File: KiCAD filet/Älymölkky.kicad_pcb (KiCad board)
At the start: 2 copper layers, 44 parts, among them P0.18_TP1 Conn_01x01_Male, U1 nRF52810-QCxx, X1 32MHz Crystal, X1_C1 12pF, X1_C2 12pF, X2 32.768 kHz Crystal, X2_C11 12pF, X2_C12 12pF

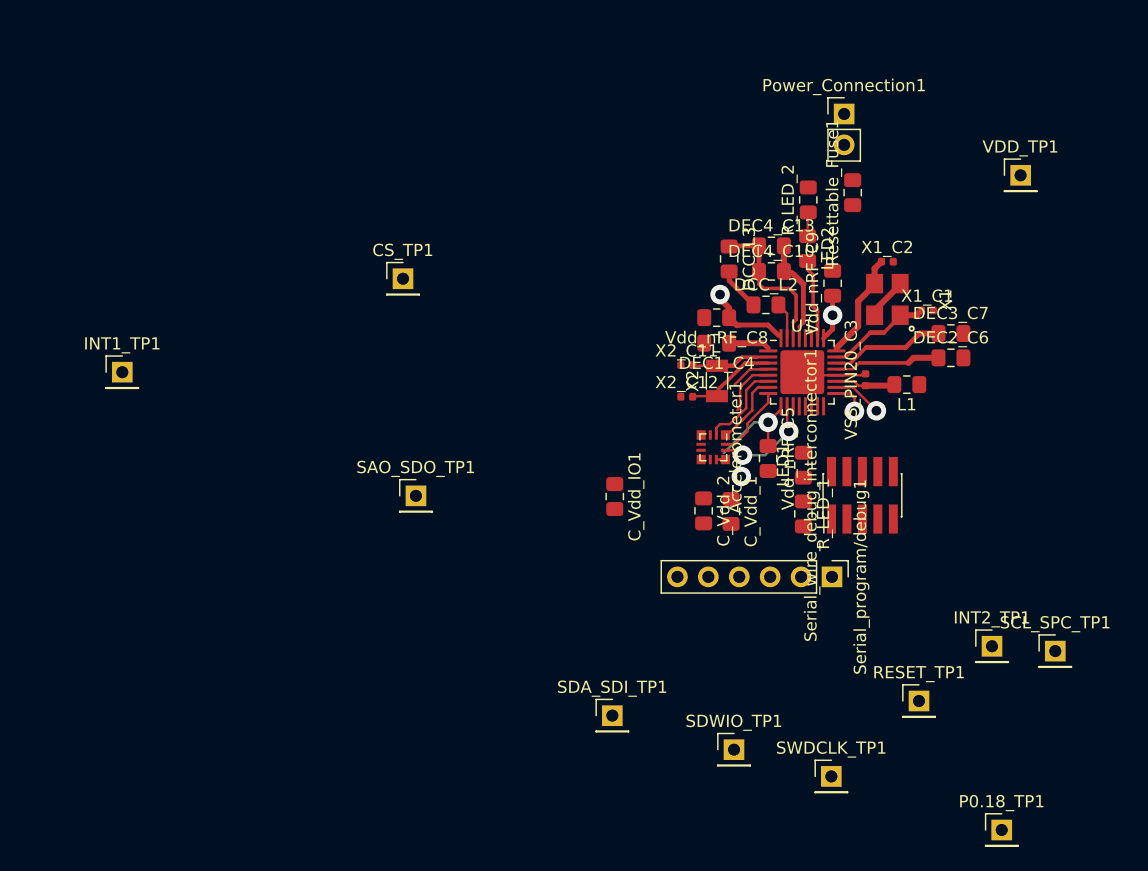
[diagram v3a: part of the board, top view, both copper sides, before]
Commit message: Drew most of remaining traces, missing antenna and switch
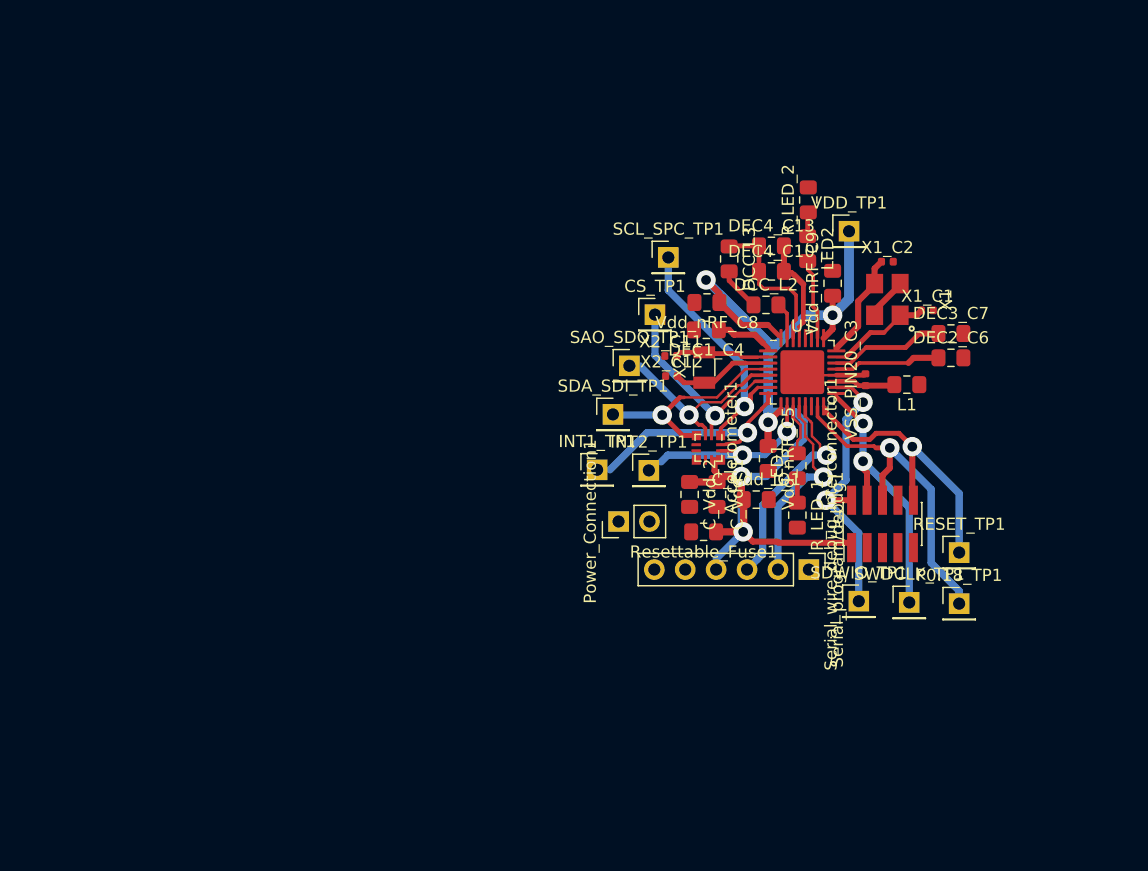
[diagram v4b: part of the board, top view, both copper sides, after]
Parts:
- moved SCL_SPC_TP1 45.4 mm to (119.8, 84.5)
- moved INT1_TP1 39.8 mm to (114.0, 102.0)
- moved Power_Connection1 38.3 mm to (115.7, 106.2), turned to 90 degrees
- moved INT2_TP1 31.7 mm to (118.2, 102.0)
- moved Resettable_Fuse1 30.4 mm to (122.7, 107.1), turned to 180 degrees
- moved SDA_SDI_TP1 24.8 mm to (115.2, 97.5)
- moved CS_TP1 20.9 mm to (118.7, 89.2)
- moved SAO_SDO_TP1 20.5 mm to (116.6, 93.5)
- moved P0.18_TP1 18.9 mm to (143.7, 113.0)
- moved SDWIO_TP1 15.9 mm to (135.4, 112.8)
- moved SWDCLK_TP1 15.7 mm to (139.6, 112.9)
- moved VDD_TP1 14.8 mm to (134.7, 82.4)
- moved RESET_TP1 12.6 mm to (143.7, 108.8)
- moved C_Vdd_IO1 11.6 mm to (127.0, 104.5), turned to 0 degrees
- moved Serial_wire_debug_interconnector1 2.87 mm to (137.4, 106.5)
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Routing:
- net VDD: track 20.3 -> 88.2 mm, vias 4 -> 5
- net /~SWO: track 0.00 -> 27.6 mm, vias 0 -> 1
- net /~Reset: track 0.00 -> 24.3 mm, vias 0 -> 1
- net /~SWDCLK: track 2.76 -> 23.0 mm, vias 1 -> 2
- net /~SWDIO: track 4.09 -> 23.8 mm, vias 1 -> 2
- net /~TX0: track 0.00 -> 17.5 mm, vias 0 -> 1
- net /~RX1: track 0.00 -> 16.6 mm, vias 0 -> 1
- net /~INT1: track 6.05 -> 21.7 mm, vias 0 -> 1
- net /~SCL_SPC: track 6.18 -> 21.5 mm, vias 0 -> 1
- net /~SDA_SDI: track 3.29 -> 18.0 mm, vias 0 -> 1
- net /~SAO_SDO: track 4.68 -> 17.1 mm, vias 0 -> 1
- net /~CS: track 7.30 -> 17.7 mm, vias 0 -> 1
- net /~INT2: track 8.79 -> 17.8 mm
- net Net-(LED1-Pad2): track 0.00 -> 4.22 mm
- net Net-(LED1-Pad1): track 0.00 -> 2.00 mm
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
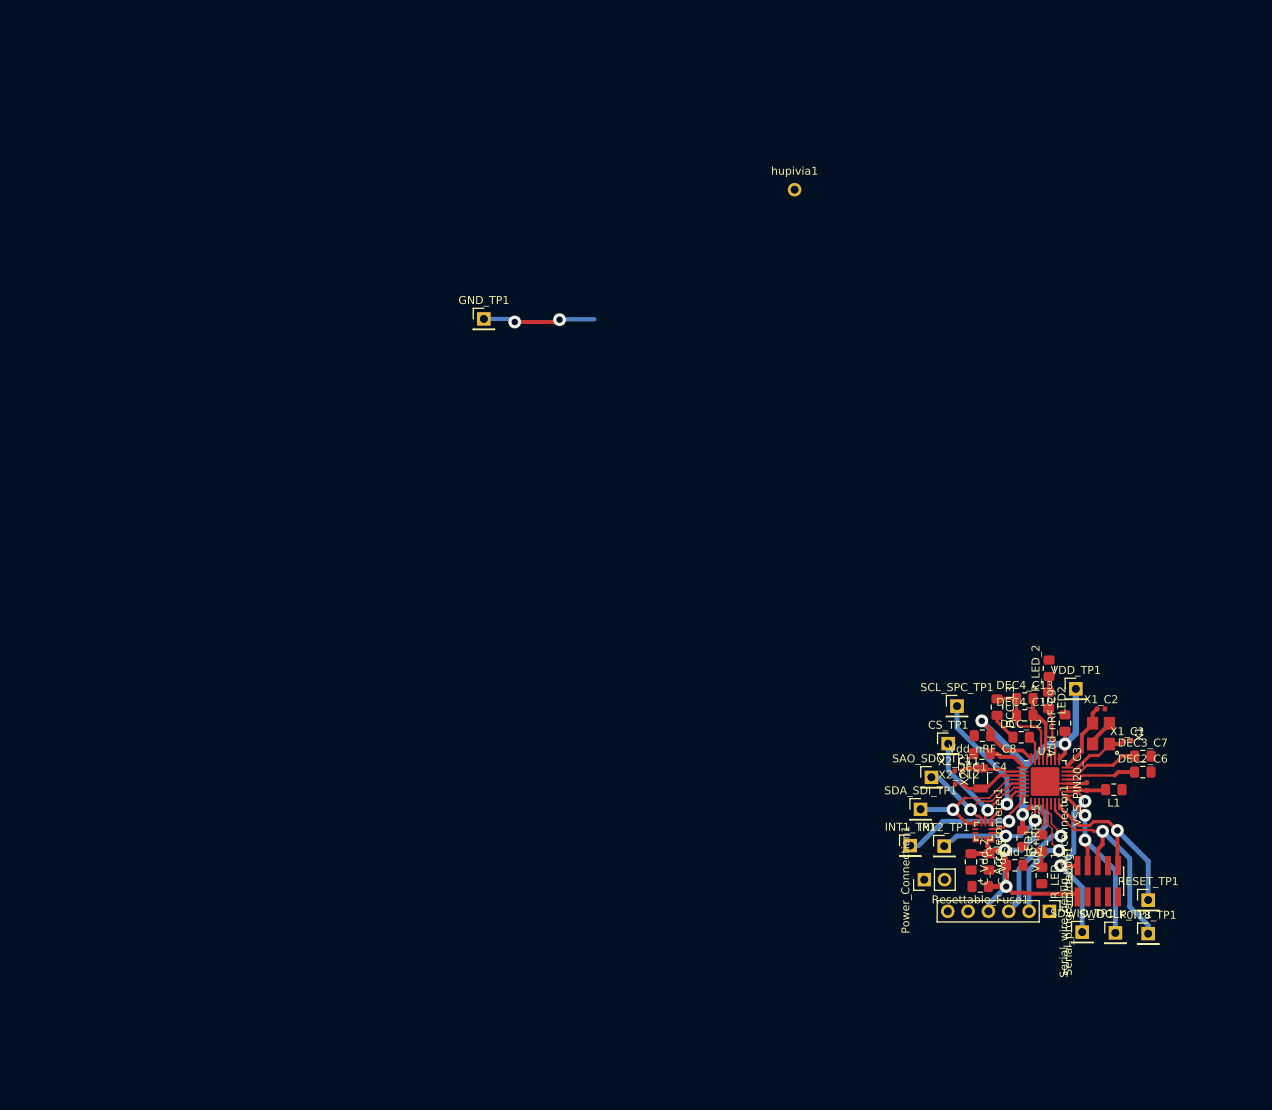
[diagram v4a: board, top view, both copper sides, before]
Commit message: Added changes made by Pyry, antenna, copper pour and slight changes
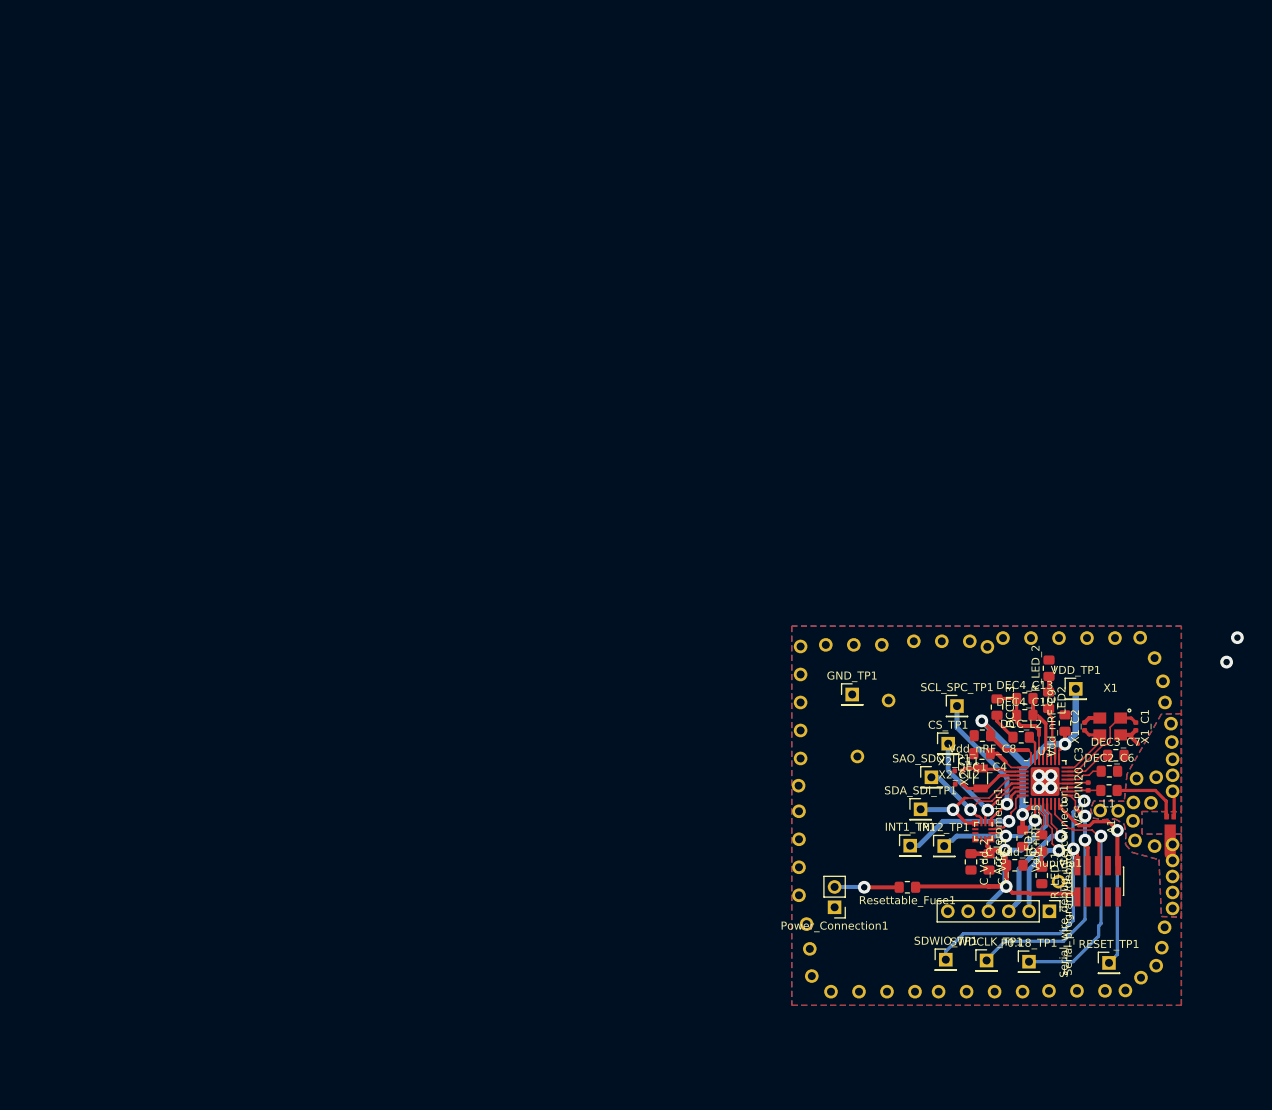
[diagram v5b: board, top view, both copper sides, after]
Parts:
- added ?: Conn_01x01_Male, Connector_PinHeader_2.54mm:PinHeader_1x01_P2.54mm_Vertical, F.Cu at (107.3, 90.8)
- added ?: Conn_01x01_Male, Connector_PinHeader_2.54mm:PinHeader_1x01_P2.54mm_Vertical, F.Cu at (101.0, 111.8)
- added ?: Conn_01x01_Male, Connector_PinHeader_2.54mm:PinHeader_1x01_P2.54mm_Vertical, F.Cu at (100.0, 94.5)
- added ?: Conn_01x01_Male, Connector_PinHeader_2.54mm:PinHeader_1x01_P2.54mm_Vertical, F.Cu at (100.0, 101.2)
- added ?: Conn_01x01_Male, Connector_PinHeader_2.54mm:PinHeader_1x01_P2.54mm_Vertical, F.Cu at (104.0, 120.2)
- added ?: Conn_01x01_Male, Connector_PinHeader_2.54mm:PinHeader_1x01_P2.54mm_Vertical, F.Cu at (107.5, 120.2)
- added ?: Conn_01x01_Male, Connector_PinHeader_2.54mm:PinHeader_1x01_P2.54mm_Vertical, F.Cu at (111.0, 120.2)
- added ?: Conn_01x01_Male, Connector_PinHeader_2.54mm:PinHeader_1x01_P2.54mm_Vertical, F.Cu at (114.5, 120.2)
- added ?: Conn_01x01_Male, Connector_PinHeader_2.54mm:PinHeader_1x01_P2.54mm_Vertical, F.Cu at (100.0, 104.7)
- added ?: Conn_01x01_Male, Connector_PinHeader_2.54mm:PinHeader_1x01_P2.54mm_Vertical, F.Cu at (117.5, 120.2)
- added ?: Conn_01x01_Male, Connector_PinHeader_2.54mm:PinHeader_1x01_P2.54mm_Vertical, F.Cu at (121.0, 120.2)
- added ?: Conn_01x01_Male, Connector_PinHeader_2.54mm:PinHeader_1x01_P2.54mm_Vertical, F.Cu at (111.2, 83.8)
- added ?: Conn_01x01_Male, Connector_PinHeader_2.54mm:PinHeader_1x01_P2.54mm_Vertical, F.Cu at (124.5, 120.2)
- added ?: Conn_01x01_Male, Connector_PinHeader_2.54mm:PinHeader_1x01_P2.54mm_Vertical, F.Cu at (128.0, 120.2)
- added ?: Conn_01x01_Male, Connector_PinHeader_2.54mm:PinHeader_1x01_P2.54mm_Vertical, F.Cu at (100.0, 108.2)
- added ?: Conn_01x01_Male, Connector_PinHeader_2.54mm:PinHeader_1x01_P2.54mm_Vertical, F.Cu at (131.3, 120.2)
- added ?: Conn_01x01_Male, Connector_PinHeader_2.54mm:PinHeader_1x01_P2.54mm_Vertical, F.Cu at (134.8, 120.2)
- added ?: Conn_01x01_Male, Connector_PinHeader_2.54mm:PinHeader_1x01_P2.54mm_Vertical, F.Cu at (138.3, 120.2)
- added ?: Conn_01x01_Male, Connector_PinHeader_2.54mm:PinHeader_1x01_P2.54mm_Vertical, F.Cu at (140.8, 120.1)
- added ?: Conn_01x01_Male, Connector_PinHeader_2.54mm:PinHeader_1x01_P2.54mm_Vertical, F.Cu at (100.2, 91.1)
- added ?: Conn_01x01_Male, Connector_PinHeader_2.54mm:PinHeader_1x01_P2.54mm_Vertical, F.Cu at (142.7, 76.0)
- added ?: Conn_01x01_Male, Connector_PinHeader_2.54mm:PinHeader_1x01_P2.54mm_Vertical, F.Cu at (100.2, 87.6)
- added ?: Conn_01x01_Male, Connector_PinHeader_2.54mm:PinHeader_1x01_P2.54mm_Vertical, F.Cu at (125.5, 76.0)
- added ?: Conn_01x01_Male, Connector_PinHeader_2.54mm:PinHeader_1x01_P2.54mm_Vertical, F.Cu at (144.5, 78.5)
- added ?: Conn_01x01_Male, Connector_PinHeader_2.54mm:PinHeader_1x01_P2.54mm_Vertical, F.Cu at (100.2, 84.1)
- added ?: Conn_01x01_Male, Connector_PinHeader_2.54mm:PinHeader_1x01_P2.54mm_Vertical, F.Cu at (100.2, 80.6)
- added ?: Conn_01x01_Male, Connector_PinHeader_2.54mm:PinHeader_1x01_P2.54mm_Vertical, F.Cu at (121.4, 76.5)
- added ?: Conn_01x01_Male, Connector_PinHeader_2.54mm:PinHeader_1x01_P2.54mm_Vertical, F.Cu at (117.9, 76.5)
- added ?: Conn_01x01_Male, Connector_PinHeader_2.54mm:PinHeader_1x01_P2.54mm_Vertical, F.Cu at (114.4, 76.5)
- added ?: Conn_01x01_Male, Connector_PinHeader_2.54mm:PinHeader_1x01_P2.54mm_Vertical, F.Cu at (145.6, 81.5)
- added ?: Conn_01x01_Male, Connector_PinHeader_2.54mm:PinHeader_1x01_P2.54mm_Vertical, F.Cu at (100.2, 77.1)
- added ?: Conn_01x01_Male, Connector_PinHeader_2.54mm:PinHeader_1x01_P2.54mm_Vertical, F.Cu at (110.4, 76.9)
- added ?: Conn_01x01_Male, Connector_PinHeader_2.54mm:PinHeader_1x01_P2.54mm_Vertical, F.Cu at (106.9, 76.9)
- added ?: Conn_01x01_Male, Connector_PinHeader_2.54mm:PinHeader_1x01_P2.54mm_Vertical, F.Cu at (129.1, 76.0)
- added ?: Conn_01x01_Male, Connector_PinHeader_2.54mm:PinHeader_1x01_P2.54mm_Vertical, F.Cu at (103.4, 76.9)
- added ?: Conn_01x01_Male, Connector_PinHeader_2.54mm:PinHeader_1x01_P2.54mm_Vertical, F.Cu at (145.8, 84.1)
- added ?: Conn_01x01_Male, Connector_PinHeader_2.54mm:PinHeader_1x01_P2.54mm_Vertical, F.Cu at (145.4, 114.8)
- added ?: Conn_01x01_Male, Connector_PinHeader_2.54mm:PinHeader_1x01_P2.54mm_Vertical, F.Cu at (144.7, 117.0)
- added ?: Conn_01x01_Male, Connector_PinHeader_2.54mm:PinHeader_1x01_P2.54mm_Vertical, F.Cu at (123.6, 77.2)
- added ?: Conn_01x01_Male, Connector_PinHeader_2.54mm:PinHeader_1x01_P2.54mm_Vertical, F.Cu at (142.8, 118.5)
- added ?: Conn_01x01_Male, Connector_PinHeader_2.54mm:PinHeader_1x01_P2.54mm_Vertical, F.Cu at (146.8, 109.8)
- added ?: Conn_01x01_Male, Connector_PinHeader_2.54mm:PinHeader_1x01_P2.54mm_Vertical, F.Cu at (146.8, 107.8)
- added ?: Conn_01x01_Male, Connector_PinHeader_2.54mm:PinHeader_1x01_P2.54mm_Vertical, F.Cu at (146.8, 105.8)
- added ?: Conn_01x01_Male, Connector_PinHeader_2.54mm:PinHeader_1x01_P2.54mm_Vertical, F.Cu at (137.7, 97.6)
- added ?: Conn_01x01_Male, Connector_PinHeader_2.54mm:PinHeader_1x01_P2.54mm_Vertical, F.Cu at (132.6, 76.0)
- added ?: Conn_01x01_Male, Connector_PinHeader_2.54mm:PinHeader_1x01_P2.54mm_Vertical, F.Cu at (146.8, 103.8)
- added ?: Conn_01x01_Male, Connector_PinHeader_2.54mm:PinHeader_1x01_P2.54mm_Vertical, F.Cu at (146.7, 89.0)
- added ?: Conn_01x01_Male, Connector_PinHeader_2.54mm:PinHeader_1x01_P2.54mm_Vertical, F.Cu at (146.6, 86.8)
- added ?: Conn_01x01_Male, Connector_PinHeader_2.54mm:PinHeader_1x01_P2.54mm_Vertical, F.Cu at (139.9, 97.7)
- added ?: Conn_01x01_Male, Connector_PinHeader_2.54mm:PinHeader_1x01_P2.54mm_Vertical, F.Cu at (144.5, 102.0)
- added ?: Conn_01x01_Male, Connector_PinHeader_2.54mm:PinHeader_1x01_P2.54mm_Vertical, F.Cu at (146.8, 95.2)
- added ?: Conn_01x01_Male, Connector_PinHeader_2.54mm:PinHeader_1x01_P2.54mm_Vertical, F.Cu at (146.8, 101.8)
- added ?: Conn_01x01_Male, Connector_PinHeader_2.54mm:PinHeader_1x01_P2.54mm_Vertical, F.Cu at (144.1, 96.7)
- added ?: Conn_01x01_Male, Connector_PinHeader_2.54mm:PinHeader_1x01_P2.54mm_Vertical, F.Cu at (146.8, 93.2)
- added ?: Conn_01x01_Male, Connector_PinHeader_2.54mm:PinHeader_1x01_P2.54mm_Vertical, F.Cu at (101.4, 114.9)
- added ?: Conn_01x01_Male, Connector_PinHeader_2.54mm:PinHeader_1x01_P2.54mm_Vertical, F.Cu at (136.1, 76.0)
- added ?: Conn_01x01_Male, Connector_PinHeader_2.54mm:PinHeader_1x01_P2.54mm_Vertical, F.Cu at (146.8, 91.2)
- added ?: Conn_01x01_Male, Connector_PinHeader_2.54mm:PinHeader_1x01_P2.54mm_Vertical, F.Cu at (141.8, 98.9)
- added ?: Conn_01x01_Male, Connector_PinHeader_2.54mm:PinHeader_1x01_P2.54mm_Vertical, F.Cu at (145.8, 112.2)
- added ?: Conn_01x01_Male, Connector_PinHeader_2.54mm:PinHeader_1x01_P2.54mm_Vertical, F.Cu at (142.2, 93.6)
- added ?: Conn_01x01_Male, Connector_PinHeader_2.54mm:PinHeader_1x01_P2.54mm_Vertical, F.Cu at (142.1, 101.3)
- added ?: Conn_01x01_Male, Connector_PinHeader_2.54mm:PinHeader_1x01_P2.54mm_Vertical, F.Cu at (144.7, 93.5)
- added ?: Conn_01x01_Male, Connector_PinHeader_2.54mm:PinHeader_1x01_P2.54mm_Vertical, F.Cu at (139.6, 76.0)
- added ?: Conn_01x01_Male, Connector_PinHeader_2.54mm:PinHeader_1x01_P2.54mm_Vertical, F.Cu at (100.0, 97.7)
- added ?: Conn_01x01_Male, Connector_PinHeader_2.54mm:PinHeader_1x01_P2.54mm_Vertical, F.Cu at (101.7, 118.3)
- added A1: ACAG0201-2450-T, ceramic_antenna_footprint:ACAG0201-2450-T, F.Cu at (146.4, 99.0)
- added hupivia1: Conn_01x01_Male, Connector_PinHeader_2.54mm:PinHeader_1x01_P2.54mm_Vertical, F.Cu at (132.5, 106.5)
- moved ? 87.5 mm to (141.8, 96.6)
- moved GND_TP1 65.7 mm to (106.7, 83.1)
- moved SDWIO_TP1 17.4 mm to (118.4, 116.2)
- moved SWDCLK_TP1 16.5 mm to (123.5, 116.3)
- moved P0.18_TP1 15.3 mm to (128.8, 116.5)
- moved Power_Connection1 11.7 mm to (104.5, 109.7), turned to 180 degrees
- moved RESET_TP1 9.25 mm to (138.8, 116.7)
- moved Resettable_Fuse1 9.10 mm to (113.6, 107.2)
- moved DEC2_C6 4.18 mm to (138.8, 92.7)
- moved DEC3_C7 3.38 mm to (139.7, 90.7)
- moved X1_C2 3.01 mm to (135.8, 87.1), turned to 90 degrees
- moved X1_C1 2.09 mm to (142.2, 87.1), turned to 270 degrees
- moved X1 1.46 mm to (138.9, 87.1), turned to 180 degrees
- moved L1 0.61 mm to (138.8, 95.1)
- moved VSS_PIN20_C3 0.20 mm to (136.2, 94.6)
- renumbered hupivia1 to ?
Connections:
- ? pad 1: /~GND -> Earth
- GND_TP1 pad 1: /~GND -> Earth
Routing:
- net /~SWDIO: track 23.8 -> 39.2 mm
- net /~GND: track 14.1 -> 0.00 mm, vias 2 -> 0
- net /~SWDCLK: track 23.0 -> 34.5 mm
- net VDD: track 88.2 -> 97.9 mm
- net /ANTENNA: track 0.00 -> 8.40 mm
- net Net-(Power_Connection1-Pad2): track 0.00 -> 8.09 mm, vias 0 -> 1
- net Earth: track 17.7 -> 25.7 mm, vias 0 -> 4
- net /~SWO: track 27.6 -> 34.5 mm
- net /~Reset: track 24.3 -> 30.9 mm
- net Net-(DEC2_C6-Pad1): track 8.78 -> 4.64 mm
- net Net-(U1-Pad23): track 8.64 -> 12.6 mm
- net Net-(DEC3_C7-Pad1): track 9.40 -> 6.06 mm
- net Net-(LED2-Pad1): track 1.97 -> 3.94 mm
- net /~INT2: track 17.8 -> 18.8 mm
- net Net-(L1-Pad2): track 4.95 -> 4.32 mm
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- added copper zone on B.Cu, net Earth
- added copper zone on F.Cu, net Earth
